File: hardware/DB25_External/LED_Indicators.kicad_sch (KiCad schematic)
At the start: 6 parts, among them U1 74HC14

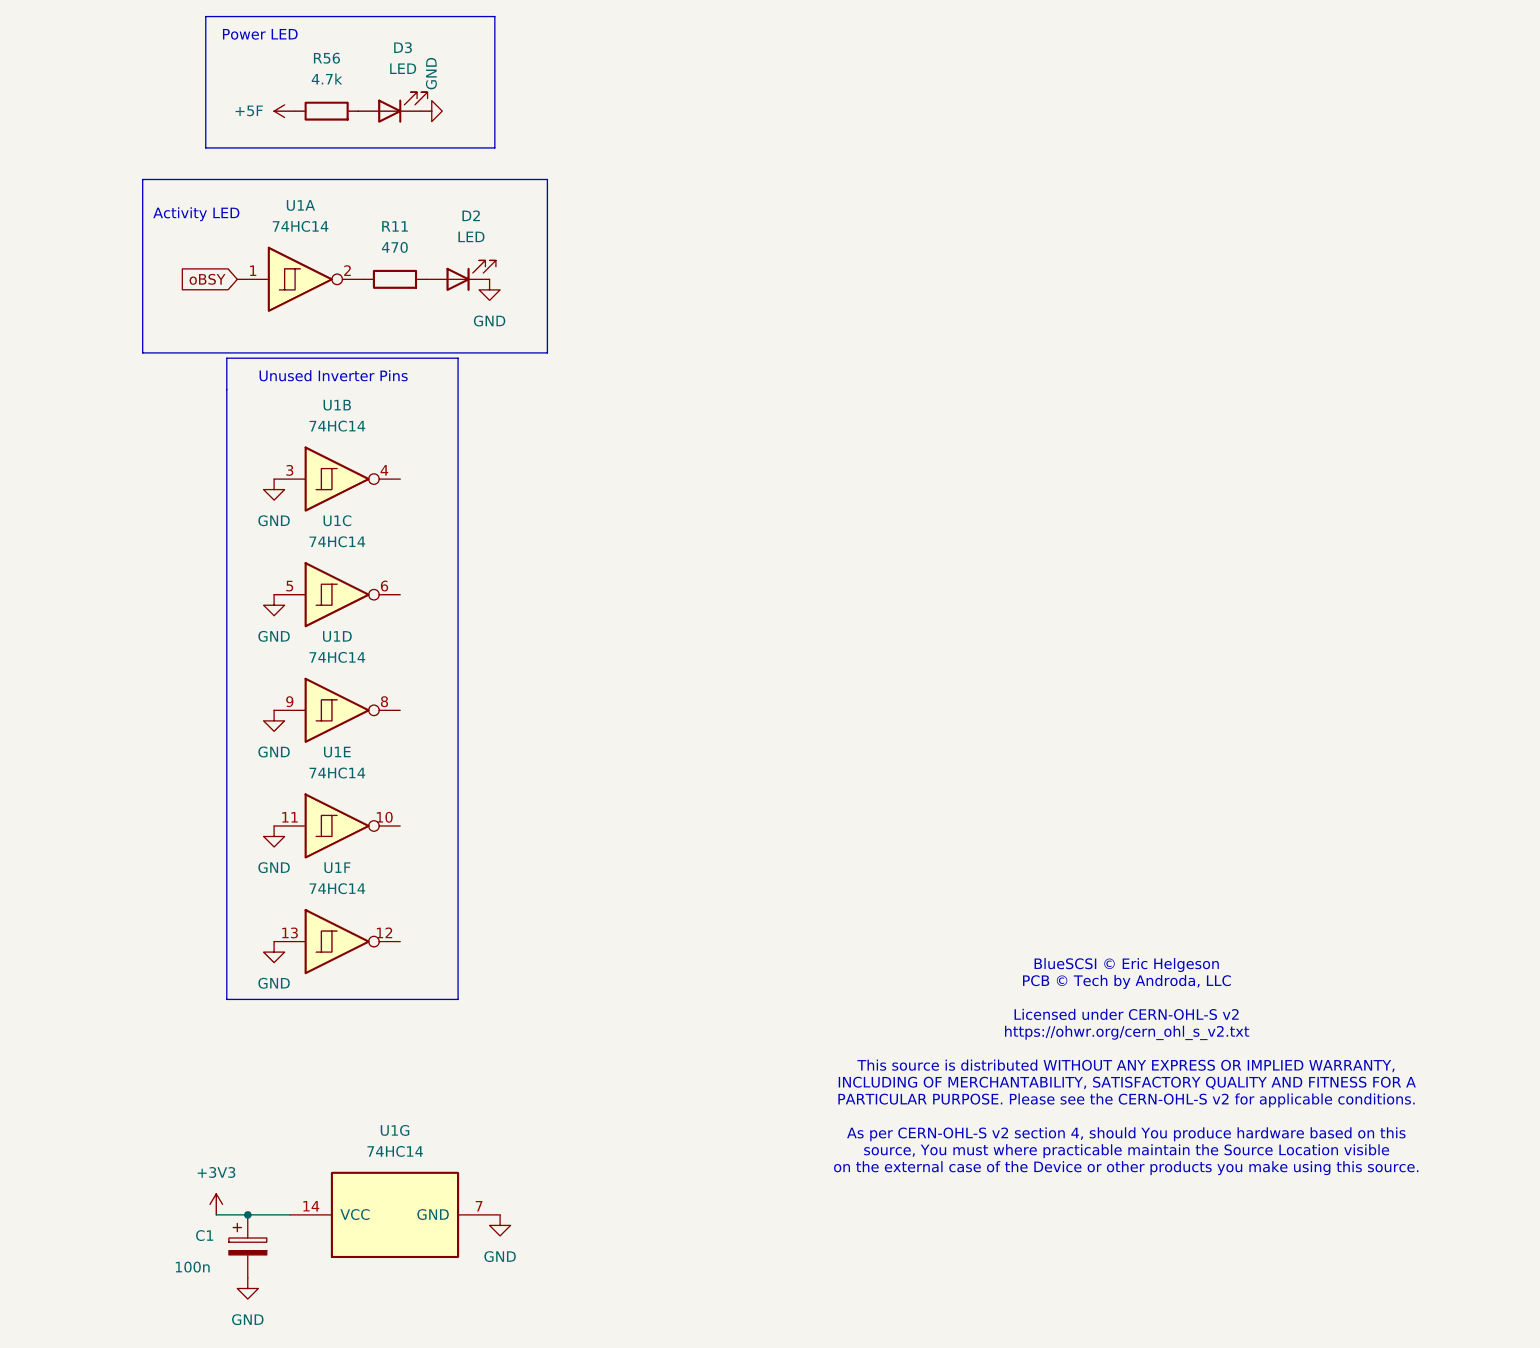
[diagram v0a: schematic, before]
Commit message: My version sent to Aisler, pico under the PCB
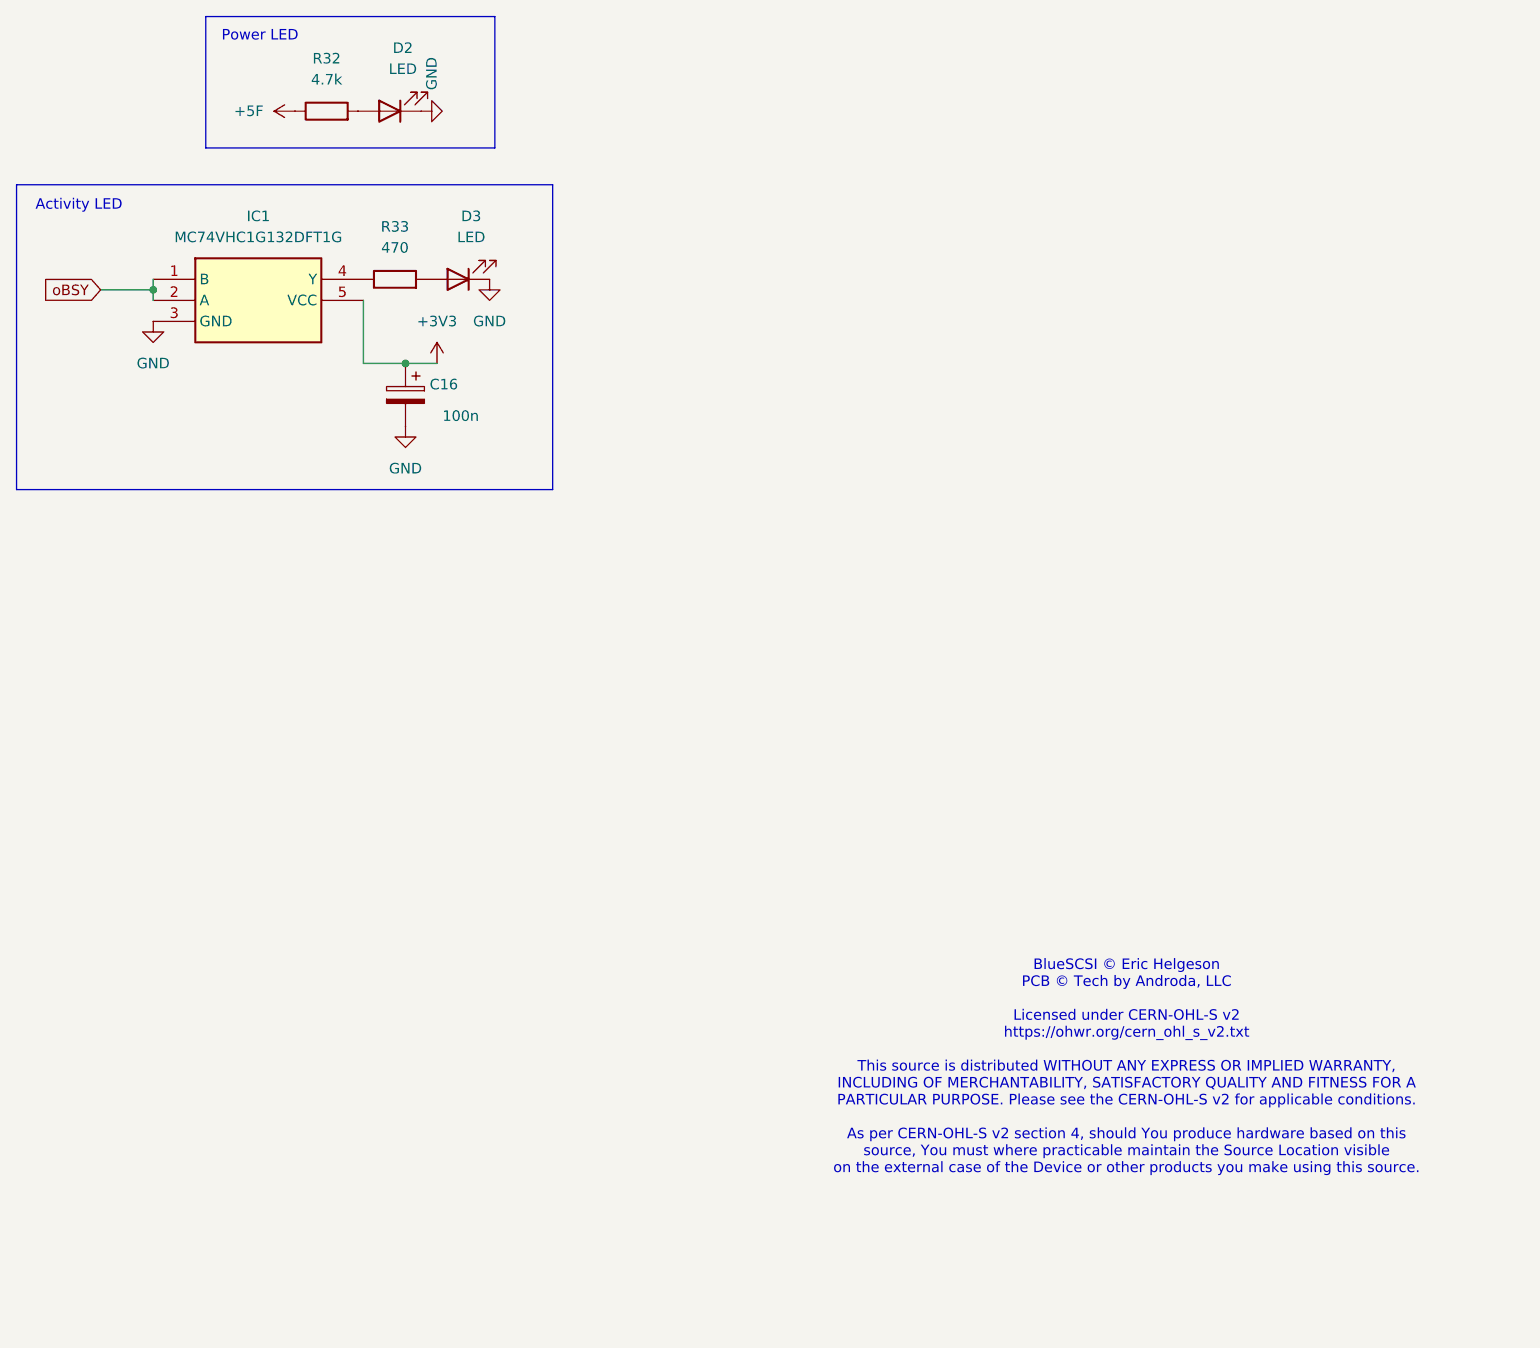
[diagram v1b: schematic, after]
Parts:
- removed U1: 74HC14, symbol 74xx:74HC14
- added IC1: MC74VHC1G132DFT1G, SOT65P210X110-5N:SOT65P210X110-5N, symbol MC74VHC1G132DFT1G:MC74VHC1G132DFT1G
- D2: renamed from D3; footprint LED_SMD:LED_0603_1608Metric_Pad1.05x0.95mm_HandSolder -> LED_SMD:LED_0805_2012Metric_Pad1.15x1.40mm_HandSolder
- D3: renamed from D2; footprint LED_SMD:LED_0603_1608Metric_Pad1.05x0.95mm_HandSolder -> LED_SMD:LED_0805_2012Metric_Pad1.15x1.40mm_HandSolder
- R32: renamed from R56; footprint Resistor_SMD:R_0603_1608Metric_Pad0.98x0.95mm_HandSolder -> Resistor_SMD:R_0805_2012Metric_Pad1.20x1.40mm_HandSolder
- R33: renamed from R11; footprint Resistor_SMD:R_0603_1608Metric_Pad0.98x0.95mm_HandSolder -> Resistor_SMD:R_0805_2012Metric_Pad1.20x1.40mm_HandSolder
- renumbered C1 to C16
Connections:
- net +3V3: now also IC1.5 (VCC)
- net GND: now also IC1.3 (GND)
- net oBSY: now also IC1.1 (B), IC1.2 (A)
- net at R33.1: now also IC1.4 (Y)
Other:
- note removed: "Unused Inverter Pins"
- moved on the sheet: C16

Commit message: Clean up
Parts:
- C16: value 100n -> 0.1uF
- R33: value 470 -> 2.2K
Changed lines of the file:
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@@
 			)
 		)
-		(property "Value" "100n"
+		(property "Value" "0.1uF"
 			(at 154.94 72.39 0)
 			(effects
@@
 			)
 		)
-		(property "Value" "470"
+		(property "Value" "2.2K"
 			(at 144.78 52.07 90)
 			(effects
